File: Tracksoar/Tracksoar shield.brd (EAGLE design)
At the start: 44 x 19.5 mm, 3 parts

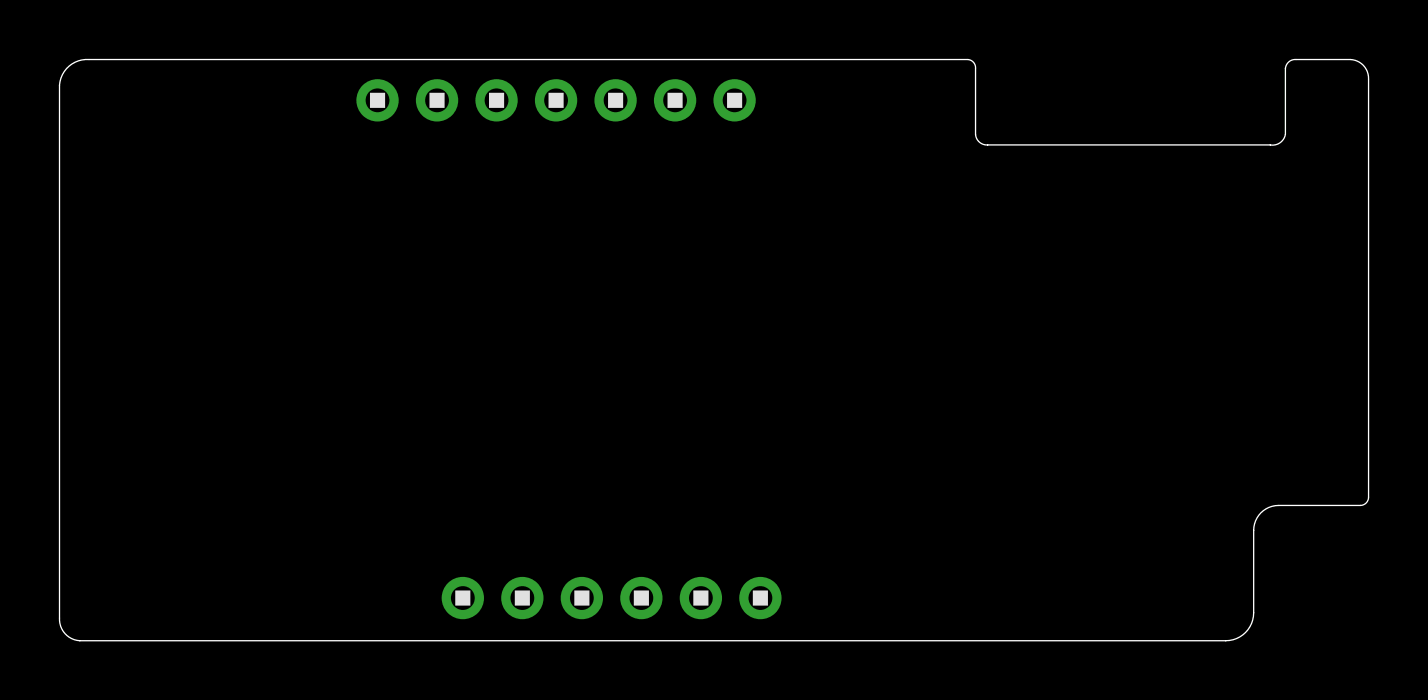
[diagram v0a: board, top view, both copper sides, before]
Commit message: fixed shield footprint
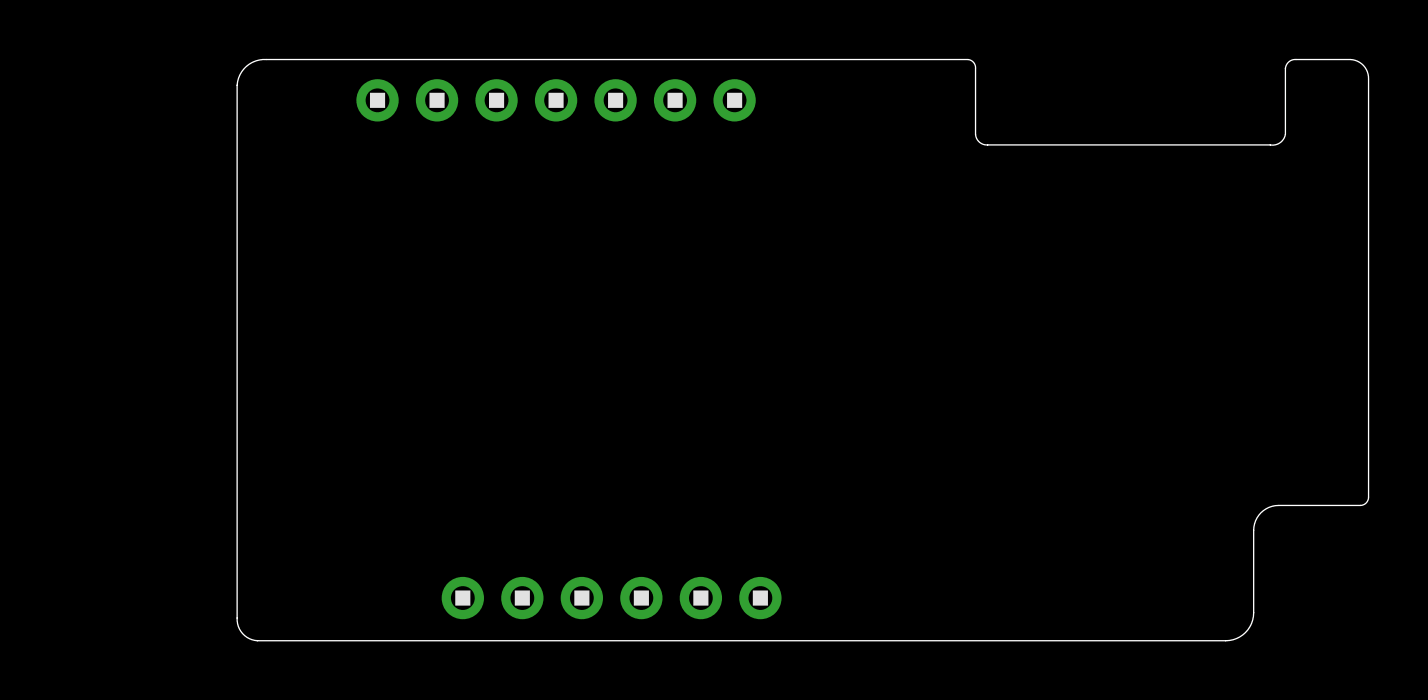
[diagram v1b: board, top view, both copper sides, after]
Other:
- board size 44 x 19.5 mm -> 38 x 19.5 mm
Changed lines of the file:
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@@
 <rectangle x1="37.4015" y1="2.7305" x2="37.9095" y2="2.7559" layer="26" rot="R180"/>
 <rectangle x1="37.5793" y1="2.7559" x2="37.7317" y2="2.7813" layer="26" rot="R180"/>
-<wire x1="0.7112" y1="0.0254" x2="0.0254" y2="0.7874" width="0" layer="20" curve="-90"/>
-<wire x1="0.0254" y1="0.7874" x2="0.0254" y2="18.6944" width="0" layer="20"/>
-<wire x1="0.0254" y1="18.6944" x2="1.016" y2="19.558" width="0" layer="20" curve="-90"/>
-<wire x1="1.016" y1="19.558" x2="30.5562" y2="19.558" width="0" layer="20"/>
+<wire x1="6.6802" y1="0.0254" x2="5.9944" y2="0.7874" width="0" layer="20" curve="-90"/>
+<wire x1="5.9944" y1="0.7874" x2="5.9944" y2="18.6944" width="0" layer="20"/>
+<wire x1="5.9944" y1="18.6944" x2="6.985" y2="19.558" width="0" layer="20" curve="-90"/>
+<wire x1="6.985" y1="19.558" x2="30.5562" y2="19.558" width="0" layer="20"/>
 <wire x1="30.5562" y1="19.558" x2="30.8102" y2="19.2532" width="0" layer="20" curve="-90"/>
 <wire x1="30.8102" y1="19.2532" x2="30.8102" y2="17.0434" width="0" layer="20"/>
@@
 <wire x1="43.4086" y1="19.558" x2="44.0182" y2="18.8976" width="0" layer="20" curve="-90"/>
 <wire x1="44.0182" y1="18.8976" x2="44.0182" y2="4.8514" width="0" layer="20"/>
-<wire x1="39.2176" y1="0.0254" x2="0.7112" y2="0.0254" width="0" layer="20"/>
+<wire x1="39.2176" y1="0.0254" x2="6.6802" y2="0.0254" width="0" layer="20"/>
 <wire x1="39.2176" y1="0.0254" x2="40.1574" y2="0.9652" width="0" layer="20" curve="90"/>
 <wire x1="40.1574" y1="0.9652" x2="40.1574" y2="3.7338" width="0" layer="20"/>
